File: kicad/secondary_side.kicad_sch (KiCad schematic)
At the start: 54 parts, among them U1 B179, U3 LM324

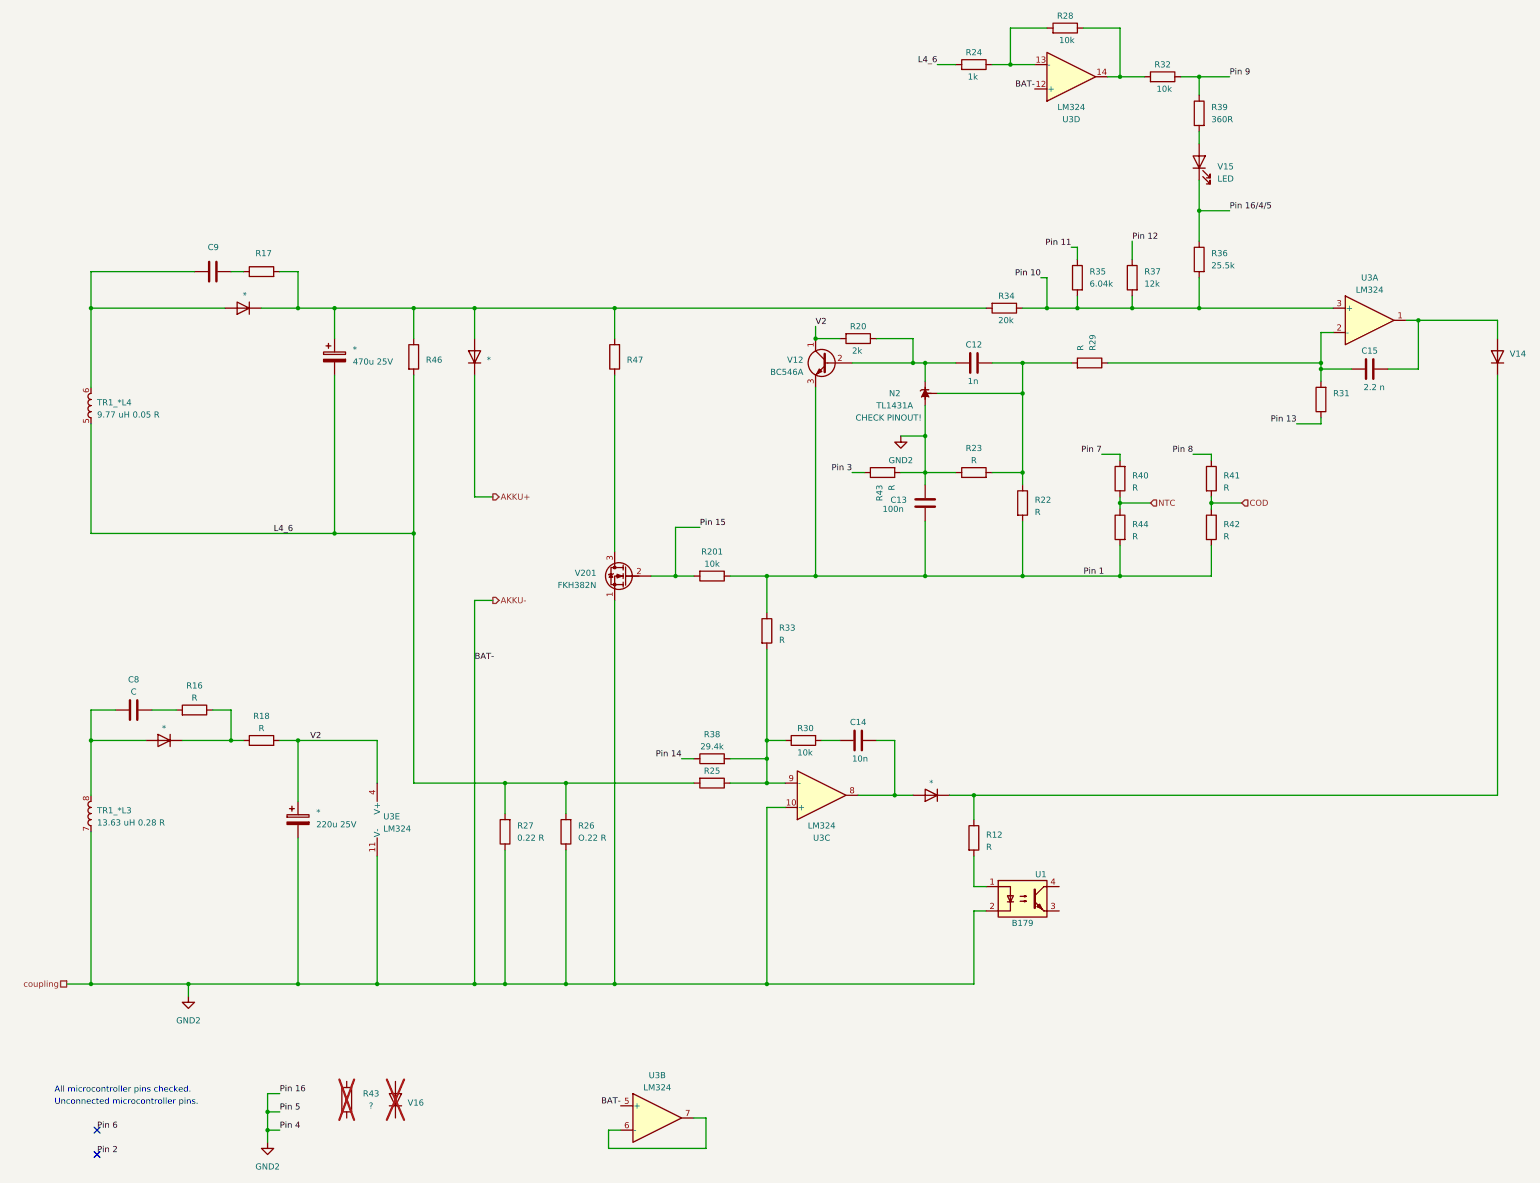
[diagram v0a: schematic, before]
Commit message: Add footprints
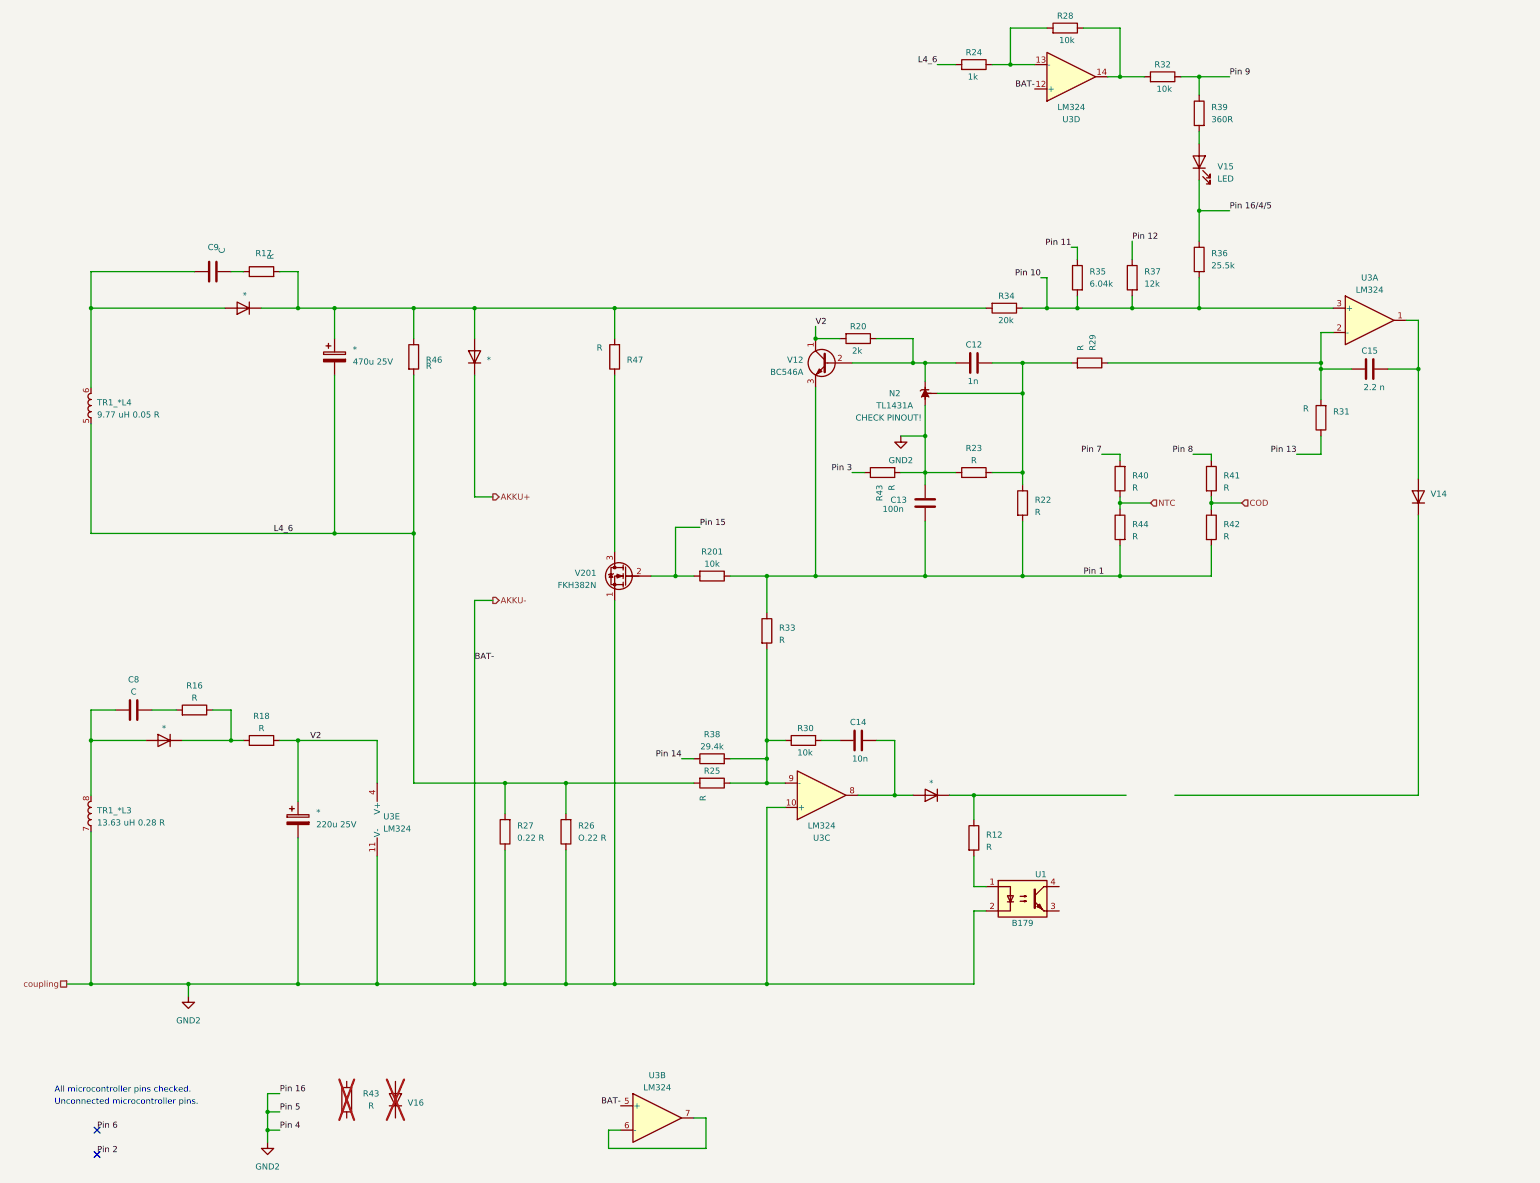
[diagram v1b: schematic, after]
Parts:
- C9: value ~ -> C
- R12, R16, R18, R20, R201, R22, R23, R24, R26, R27, R28, R29, R30, R32, R33, R34, R35, R36, R37, R38, R39, R40, R41, R42, R43, R44: footprint (none) -> Resistor_THT:R_Axial_DIN0207_L6.3mm_D2.5mm_P10.16mm_Horizontal
- R17, R25, R31, R46, R47: value ~ -> R; footprint (none) -> Resistor_THT:R_Axial_DIN0207_L6.3mm_D2.5mm_P10.16mm_Horizontal
- R43: value ? -> R; footprint (none) -> Resistor_THT:R_Axial_DIN0207_L6.3mm_D2.5mm_P10.16mm_Horizontal
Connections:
- net at *.1 (K), R12.1: no longer V14.1 (K)
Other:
- moved on the sheet: R31, V14

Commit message: Fix symbol names
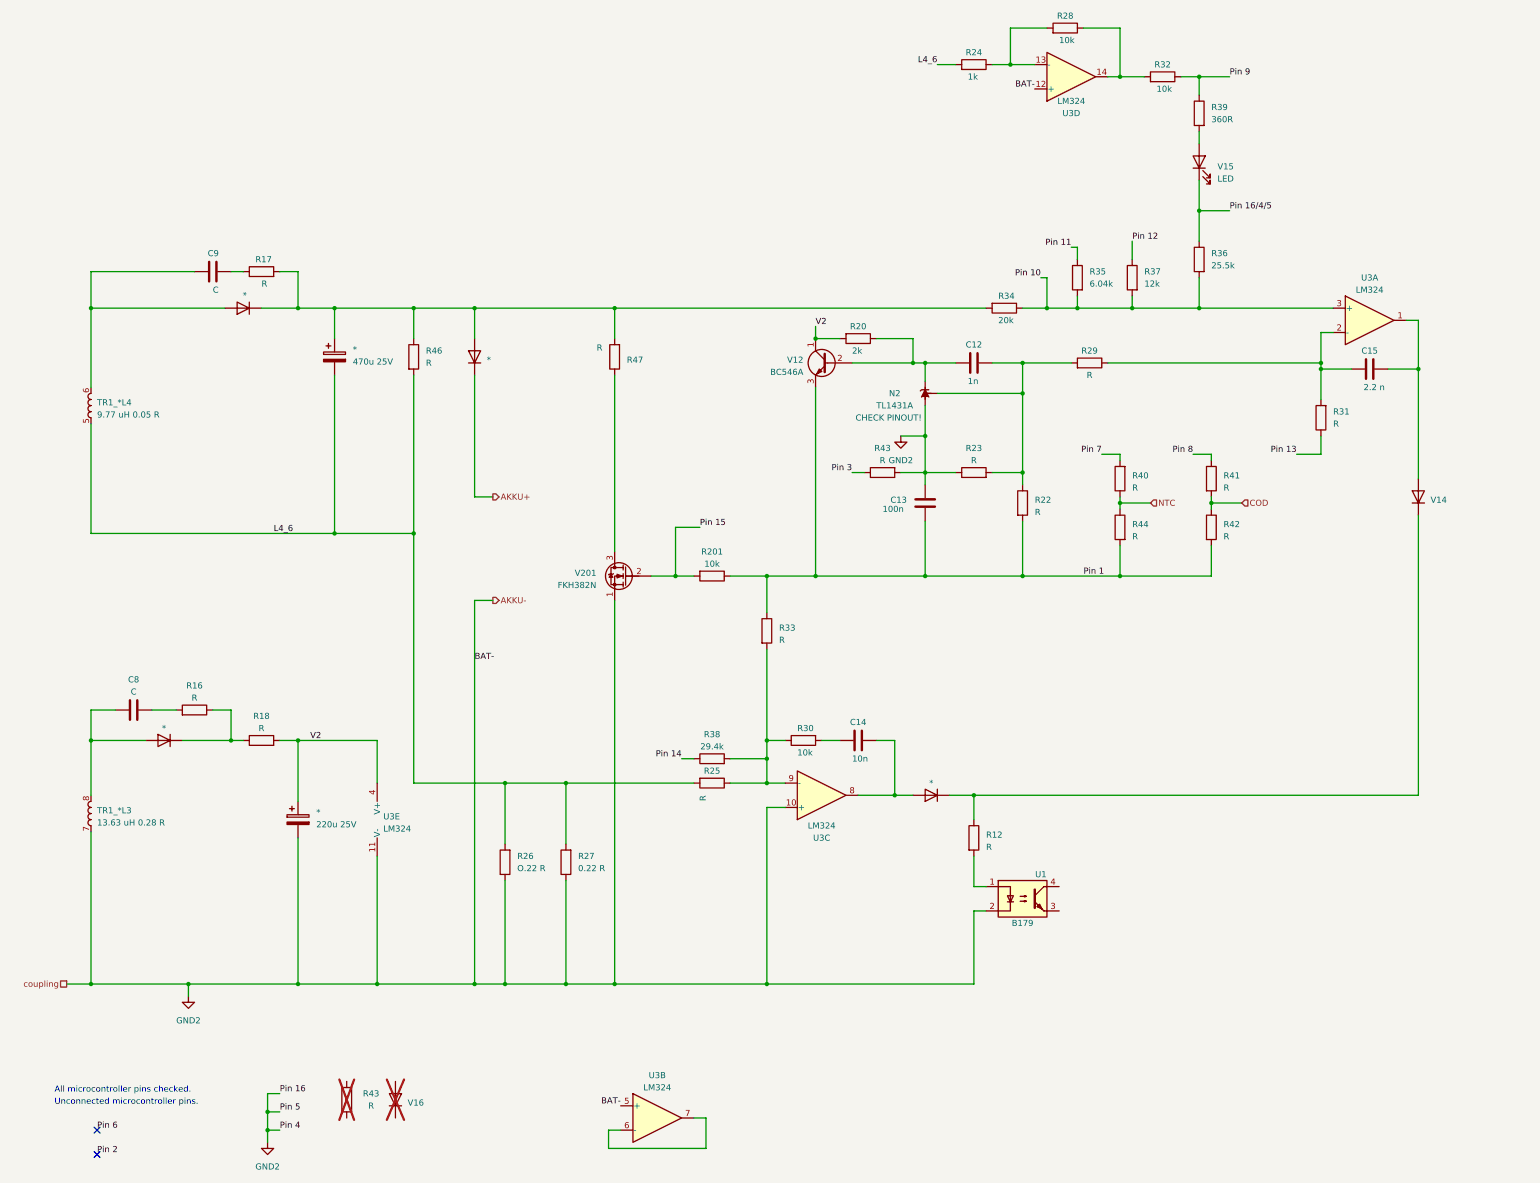
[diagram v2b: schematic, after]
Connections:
- net at V14.1 (K): now also *.1 (K), R12.1
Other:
- moved on the sheet: R26, R27
